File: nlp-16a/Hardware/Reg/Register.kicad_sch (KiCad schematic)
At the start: 32 parts, among them U10 CD74HC00, U11 CD74HC00, U12 CD74HC00, U13 CD74HC00, U14 CD74HC00, U15 CD74HC00, U16 CD74HC00, U33 CD74HC00, U34 CD74HC00, U9 CD74HC00

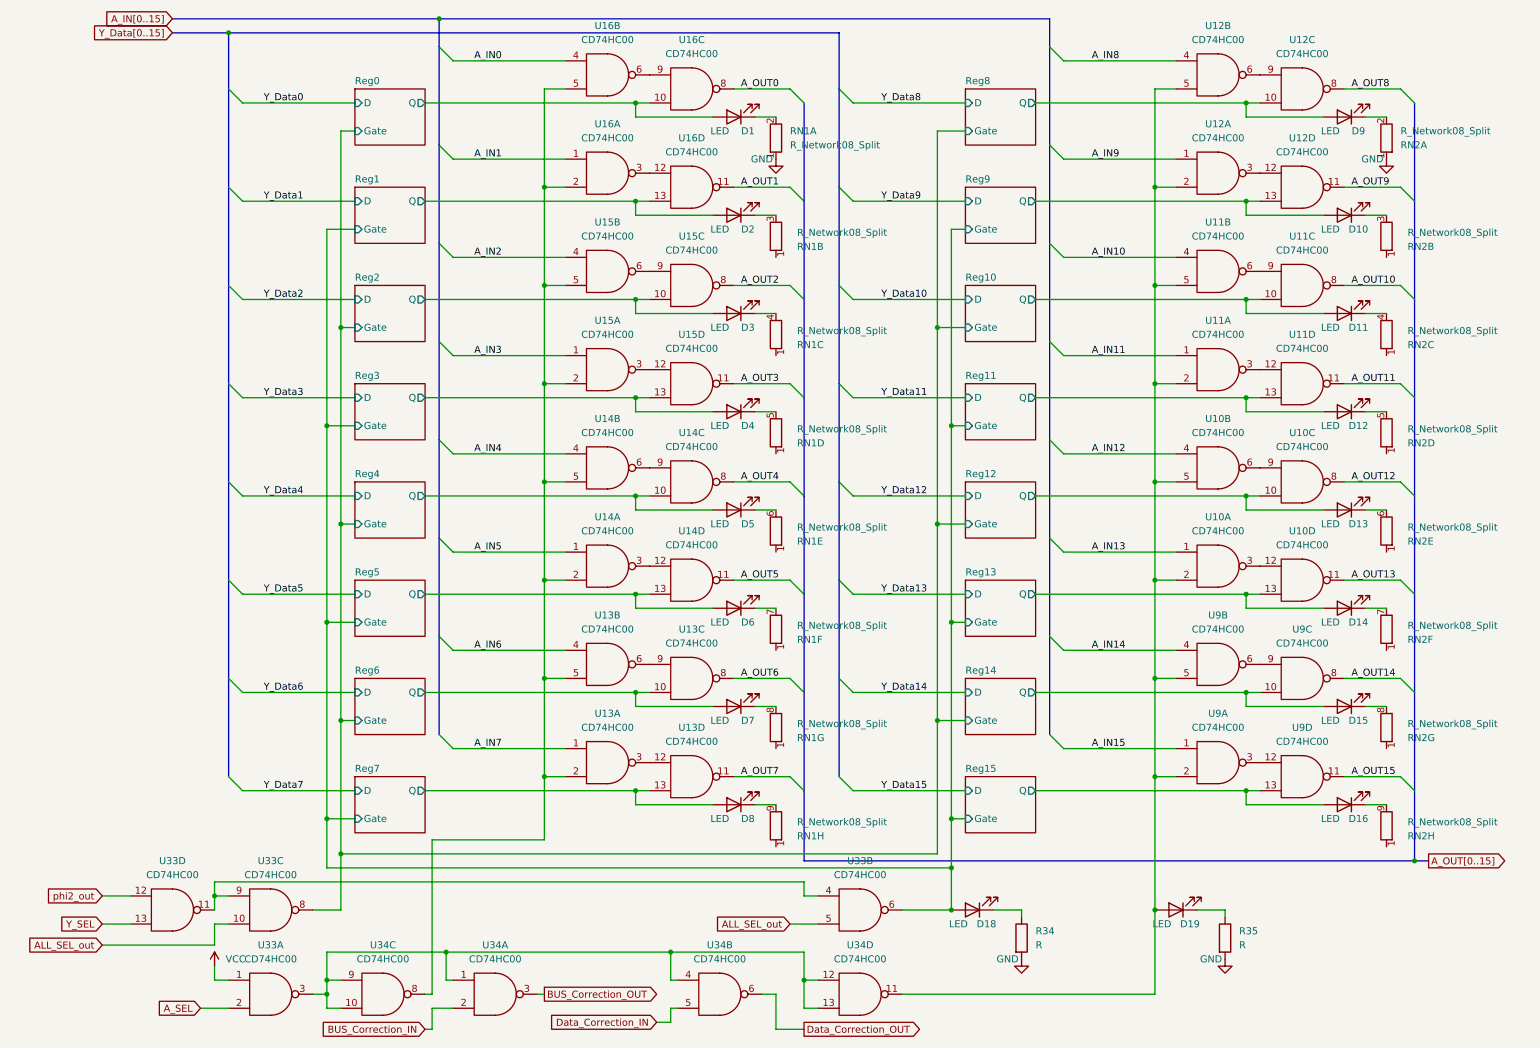
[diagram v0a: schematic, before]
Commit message: レジスタ基板だいたい完成
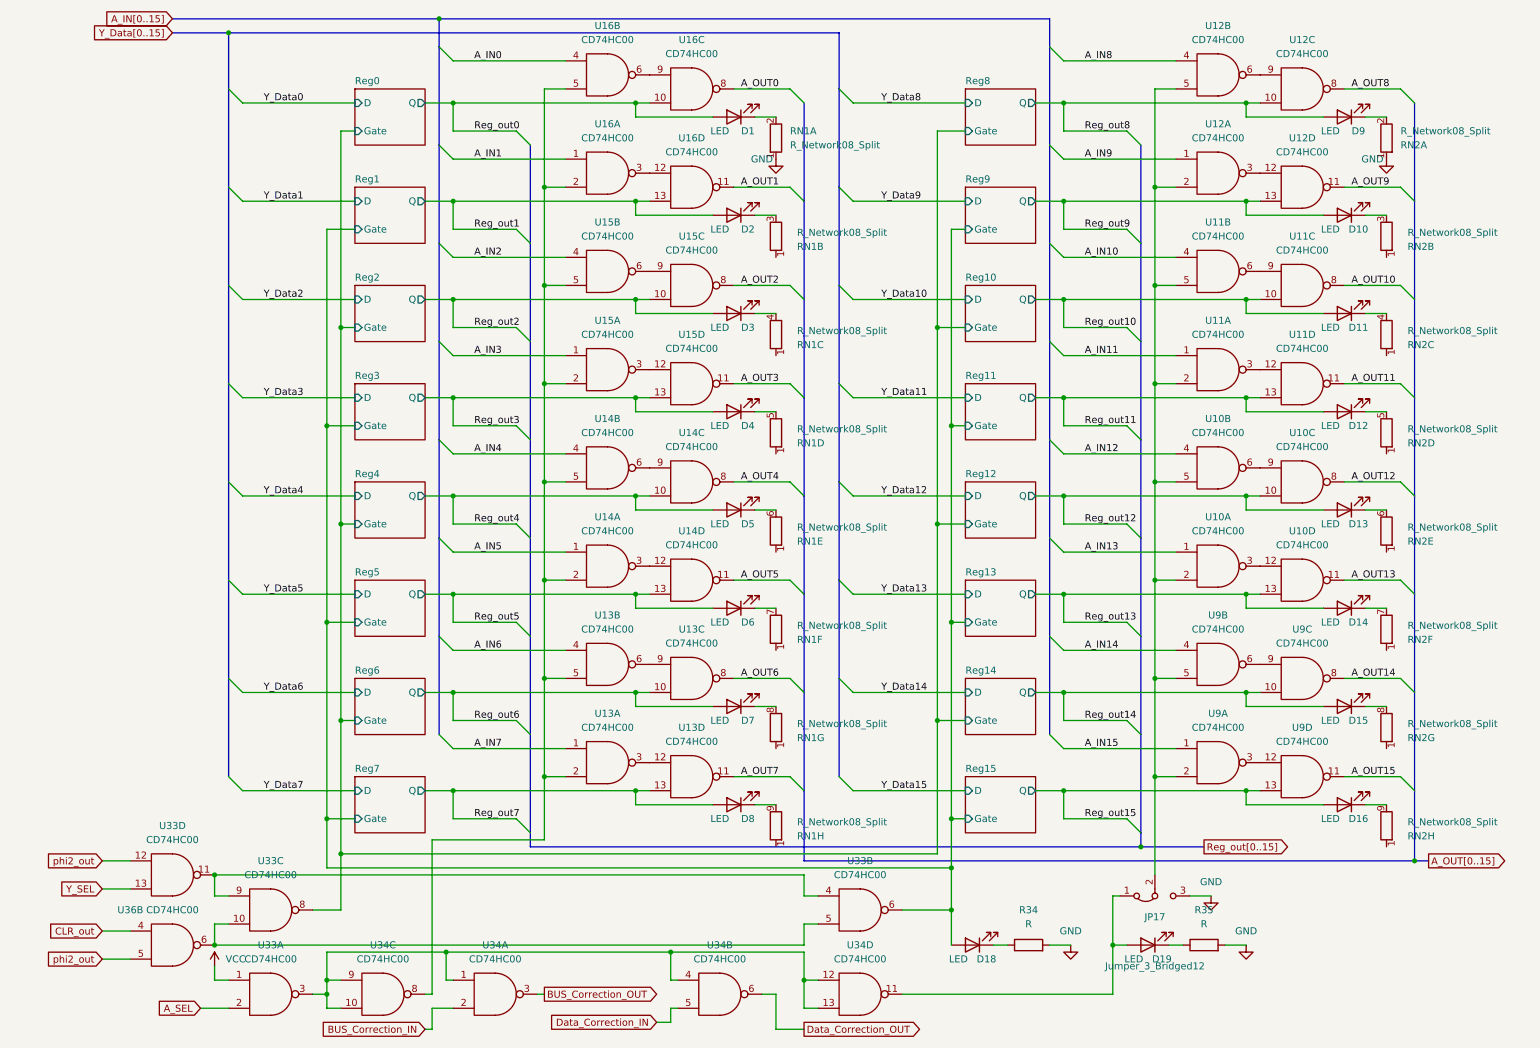
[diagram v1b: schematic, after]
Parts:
- added JP17: Jumper_3_Bridged12, Jumper:SolderJumper-3_P1.3mm_Bridged12_RoundedPad1.0x1.5mm_NumberLabels, symbol Jumper:Jumper_3_Bridged12
- added U36: CD74HC00, Package_DIP:DIP-14_W7.62mm, symbol CD74HCXX:CD74HC00
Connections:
- net GND: now also JP17.3 (B), U36.7 (GND)
- net VCC: now also U36.14 (VCC)
- net phi2_out: now also U36.5
- net at U10.2, U10.5, U11.2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: now also JP17.2 (C); no longer D19.2 (A), U34.11
- net ALL_SEL_out: no longer names the net of U33.10, U33.5
- net ALL_SEL_out: now also U36.6
- net Reg0/Q renamed Reg_out0
- net Reg1/Q renamed Reg_out1
- net Reg10/Q renamed Reg_out10
- net Reg11/Q renamed Reg_out11
- net Reg12/Q renamed Reg_out12
- net Reg13/Q renamed Reg_out13
- net Reg14/Q renamed Reg_out14
- net Reg15/Q renamed Reg_out15
- net Reg2/Q renamed Reg_out2
- net Reg3/Q renamed Reg_out3
- net Reg4/Q renamed Reg_out4
- net Reg5/Q renamed Reg_out5
- net Reg6/Q renamed Reg_out6
- net Reg7/Q renamed Reg_out7
- net Reg8/Q renamed Reg_out8
- net Reg9/Q renamed Reg_out9
- new net: D19.2 (A), JP17.1 (A), U34.11
- new net CLR_out: U36.4
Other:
- moved on the sheet: D18, D19, R34, R35, U33D

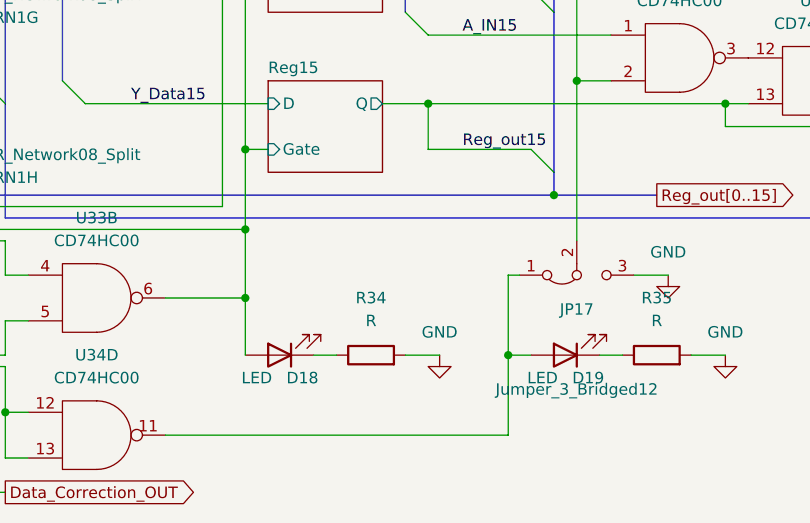
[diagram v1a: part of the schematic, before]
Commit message: テストを受けてレジスタの設計を更新
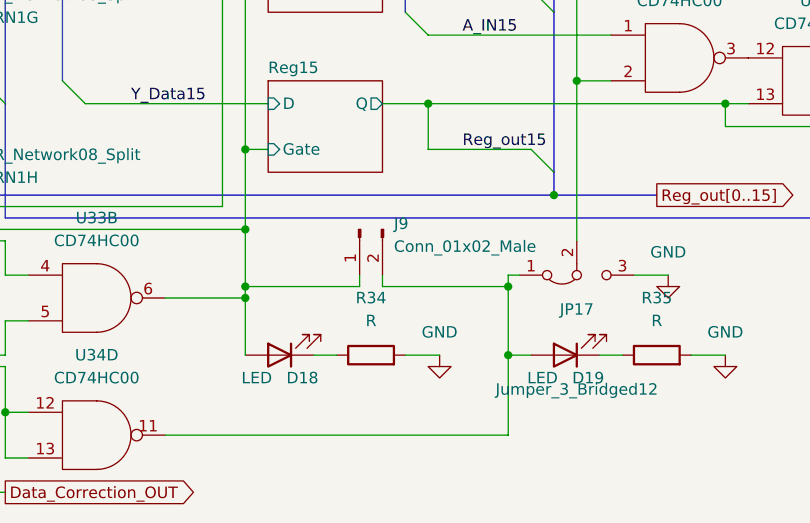
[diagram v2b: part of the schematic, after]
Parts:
- added J9: Conn_01x02_Male, Connector_PinHeader_2.54mm:PinHeader_1x02_P2.54mm_Horizontal, symbol Connector:Conn_01x02_Male
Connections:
- net Reg1/Gate: now also J9.1 (Pin_1)
- net at D19.2 (A), JP17.1 (A), U34.11: now also J9.2 (Pin_2)
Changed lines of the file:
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@@
   (junction (at 217.17 97.79) (diameter 0) (color 0 0 0 0)
   )
+  (junction (at 209.55 173.99) (diameter 0) (color 0 0 0 0)
+  )
   (junction (at 69.85 105.41) (diameter 0) (color 0 0 0 0)
   )
@@
   (junction (at 88.9 182.88) (diameter 0) (color 0 0 0 0)
   )
+  (junction (at 180.34 173.99) (diameter 0) (color 0 0 0 0)
+  )
   (junction (at 200.66 118.11) (diameter 0) (color 0 0 0 0)
   )
@@
     (stroke (width 0) (type default) (color 0 0 0 0))
   )
+  (wire (pts (xy 180.34 173.99) (xy 180.34 167.64))
+    (stroke (width 0) (type default) (color 0 0 0 0))
+  )
   (wire (pts (xy 106.68 26.67) (xy 106.68 44.45))
     (stroke (width 0) (type default) (color 0 0 0 0))
@@
     (stroke (width 0) (type default) (color 0 0 0 0))
   )
+  (wire (pts (xy 180.34 173.99) (xy 193.04 173.99))
+    (stroke (width 0) (type default) (color 0 0 0 0))
+  )
   (wire (pts (xy 153.67 196.85) (xy 148.59 196.85))
     (stroke (width 0) (type default) (color 0 0 0 0))
@@
     (stroke (width 0) (type default) (color 0 0 0 0))
   )
-  (wire (pts (xy 209.55 172.72) (xy 209.55 181.61))
+  (wire (pts (xy 209.55 172.72) (xy 209.55 173.99))
     (stroke (width 0) (type default) (color 0 0 0 0))
   )
@@
     (stroke (width 0) (type default) (color 0 0 0 0))
   )
+  (wire (pts (xy 195.58 172.72) (xy 195.58 173.99))
+    (stroke (width 0) (type default) (color 0 0 0 0))
+  )
   (wire (pts (xy 52.07 46.99) (xy 72.39 46.99))
     (stroke (width 0) (type default) (color 0 0 0 0))
@@
     (stroke (width 0) (type default) (color 0 0 0 0))
   )
+  (wire (pts (xy 193.04 172.72) (xy 193.04 173.99))
+    (stroke (width 0) (type default) (color 0 0 0 0))
+  )
   (wire (pts (xy 233.68 82.55) (xy 236.22 82.55))
     (stroke (width 0) (type default) (color 0 0 0 0))
@@
     (stroke (width 0) (type default) (color 0 0 0 0))
   )
+  (wire (pts (xy 209.55 173.99) (xy 209.55 181.61))
+    (stroke (width 0) (type default) (color 0 0 0 0))
+  )
   (wire (pts (xy 123.19 31.75) (xy 123.19 29.21))
     (stroke (width 0) (type default) (color 0 0 0 0))
@@
     (stroke (width 0) (type default) (color 0 0 0 0))
   )
-  (wire (pts (xy 180.34 175.26) (xy 180.34 167.64))
+  (wire (pts (xy 180.34 175.26) (xy 180.34 173.99))
     (stroke (width 0) (type default) (color 0 0 0 0))
   )
@@
   )
   (wire (pts (xy 90.17 100.33) (xy 123.19 100.33))
+    (stroke (width 0) (type default) (color 0 0 0 0))
+  )
+  (wire (pts (xy 195.58 173.99) (xy 209.55 173.99))
     (stroke (width 0) (type default) (color 0 0 0 0))
   )
@@
     (pin "1")
   )
+  (symbol (lib_id "Connector:Conn_01x02_Male") (at 193.04 167.64 90) (mirror x) (unit 1)
+    (in_bom yes) (on_board yes) (fields_autoplaced)
+    (property "Reference" "J9" (id 0) (at 196.85 167.0049 90)
+      (effects (font (size 1.27 1.27)) (justify right))
+    )
+    (property "Value" "Conn_01x02_Male" (id 1) (at 196.85 169.5449 90)
+      (effects (font (size 1.27 1.27)) (justify right))
+    )
+    (property "Footprint" "Connector_PinHeader_2.54mm:PinHeader_1x02_P2.54mm_Horizontal" (id 2) (at 193.04 167.64 0)
+      (effects (font (size 1.27 1.27)) hide)
+    )
+    (property "Datasheet" "~" (id 3) (at 193.04 167.64 0)
+      (effects (font (size 1.27 1.27)) hide)
+    )
+    (pin "1")
+    (pin "2")
+  )
   (symbol (lib_id "Device:LED") (at 251.46 120.65 180) (unit 1)

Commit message: レジスタクリア時の動作を修正
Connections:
- net CLR_out renamed CLR
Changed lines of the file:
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@@
     )
   )
-  (global_label "CLR_out" (shape input) (at 26.67 179.07 180) (fields_autoplaced)
+  (global_label "CLR" (shape input) (at 26.67 179.07 180) (fields_autoplaced)
     (effects (font (size 1.27 1.27)) (justify right))
-    (property "Intersheet References" "${INTERSHEET_REFS}" (id 0) (at 16.6974 178.9906 0)
+    (property "Intersheet References" "${INTERSHEET_REFS}" (id 0) (at 20.6888 178.9906 0)
       (effects (font (size 1.27 1.27)) (justify right) hide)
     )

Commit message: Reg更新
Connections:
- net A_IN0: now also U16.10; no longer U16.4
- net A_IN1: now also U16.13; no longer U16.1
- net A_IN10: now also U11.10; no longer U11.4
- net A_IN11: now also U11.13; no longer U11.1
- net A_IN12: now also U10.10; no longer U10.4
- net A_IN13: now also U10.13; no longer U10.1
- net A_IN14: now also U9.10; no longer U9.4
- net A_IN15: now also U9.13; no longer U9.1
- net A_IN2: now also U15.10; no longer U15.4
- net A_IN3: now also U15.13; no longer U15.1
- net A_IN4: now also U14.10; no longer U14.4
- net A_IN5: now also U14.13; no longer U14.1
- net A_IN6: now also U13.10; no longer U13.4
- net A_IN7: now also U13.13; no longer U13.1
- net A_IN8: now also U12.10; no longer U12.4
- net A_IN9: now also U12.13; no longer U12.1
- net Reg_out0: now also U16.5; no longer U16.10
- net Reg_out1: now also U16.2; no longer U16.13
- net Reg_out10: now also U11.5; no longer U11.10
- net Reg_out11: now also U11.2; no longer U11.13
- net Reg_out12: now also U10.5; no longer U10.10
- net Reg_out13: now also U10.2; no longer U10.13
- net Reg_out14: now also U9.5; no longer U9.10
- net Reg_out15: now also U9.2; no longer U9.13
- net Reg_out2: now also U15.5; no longer U15.10
- net Reg_out3: now also U15.2; no longer U15.13
- net Reg_out4: now also U14.5; no longer U14.10
- net Reg_out5: now also U14.2; no longer U14.13
- net Reg_out6: now also U13.5; no longer U13.10
- net Reg_out7: now also U13.2; no longer U13.13
- net Reg_out8: now also U12.5; no longer U12.10
- net Reg_out9: now also U12.2; no longer U12.13
- new net: JP17.2 (C), U10.1, U10.4, U11.1, U11.4, U12.1, U12.4, U9.1, U9.4
- new net: U13.1, U13.4, U14.1, U14.4, U15.1, U15.4, U16.1, U16.4, U34.8
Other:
- moved on the sheet: D1, D10, D11, D12, D13, D14, D15, D16, D2, D3, D4, D5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
